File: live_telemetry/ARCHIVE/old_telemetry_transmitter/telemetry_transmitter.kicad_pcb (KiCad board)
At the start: 2 copper layers, 48.3 x 38.1 mm, 42 parts, among them J1 Programming Header, J2 BUS_CONN, J5 RFD900x, Q1 PJA3405, Q2 TSM2306CX, U1 PIC18F26K83, U2 MCP2562, U3 SPX3819M5-L-3-3/TR, U5 INA180, U6 AP1509-50SG-13, Y1 Crystal

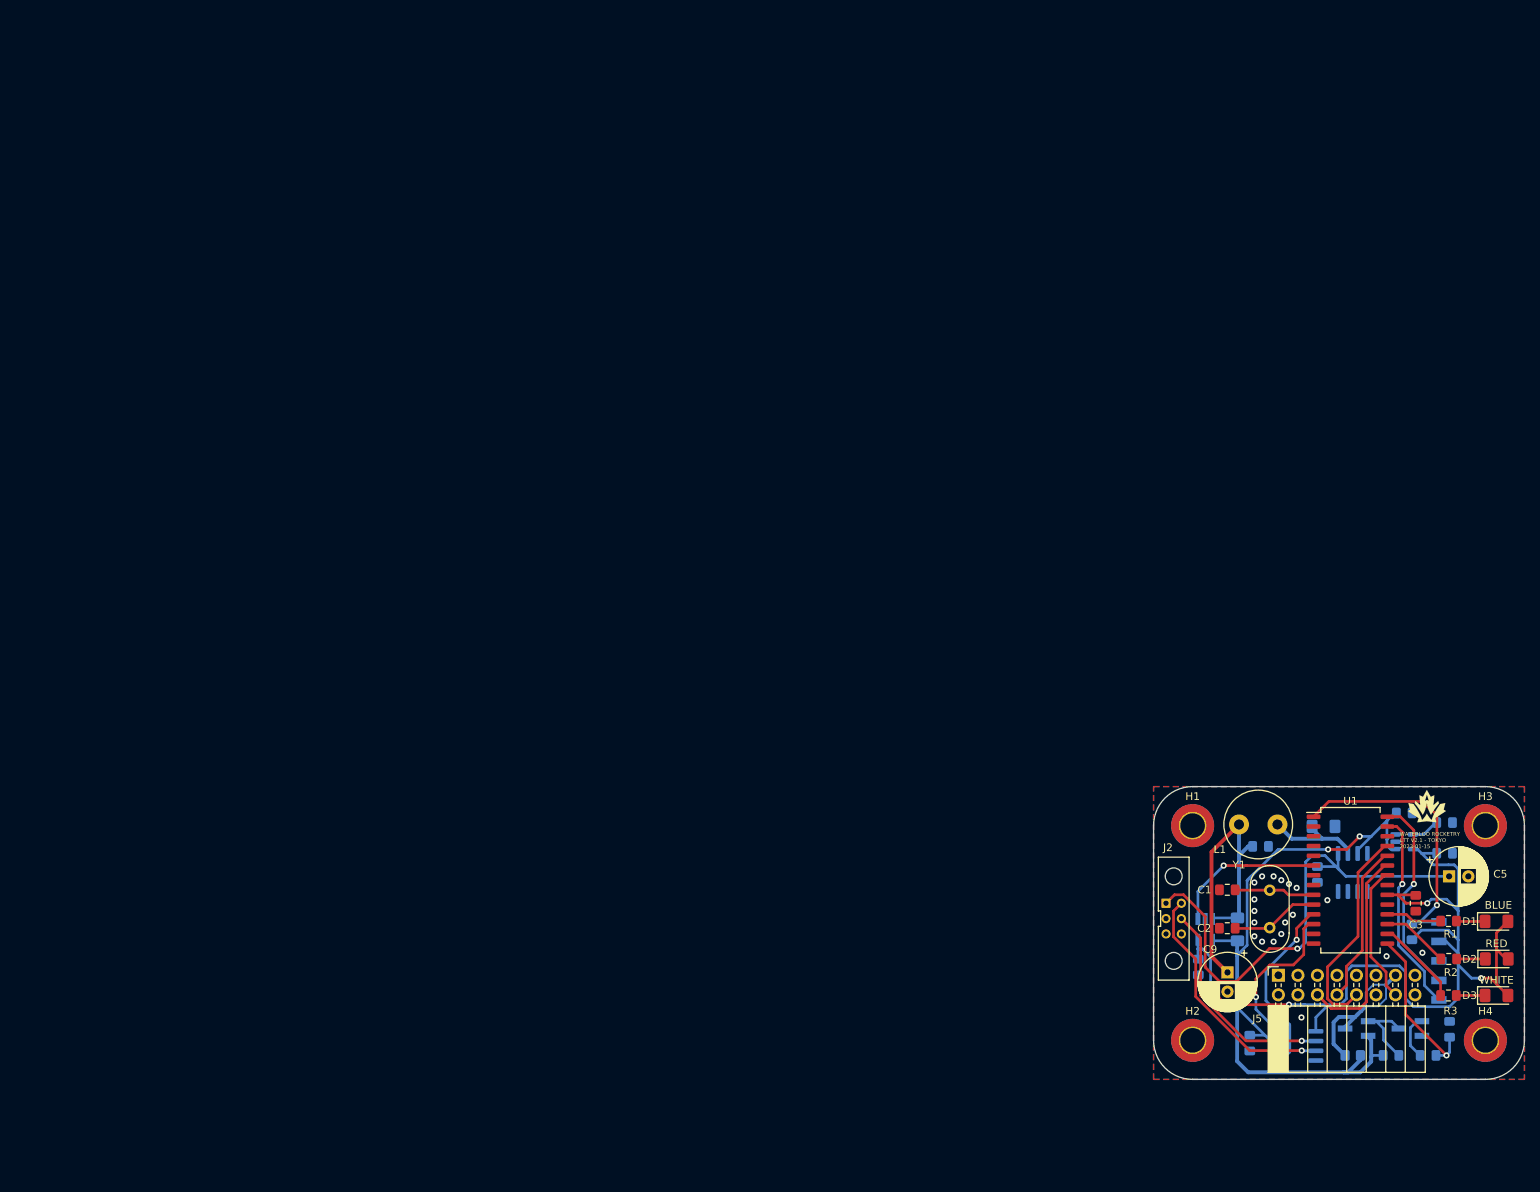
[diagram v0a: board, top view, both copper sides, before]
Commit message: add crystal and LDO datasheets, start layout
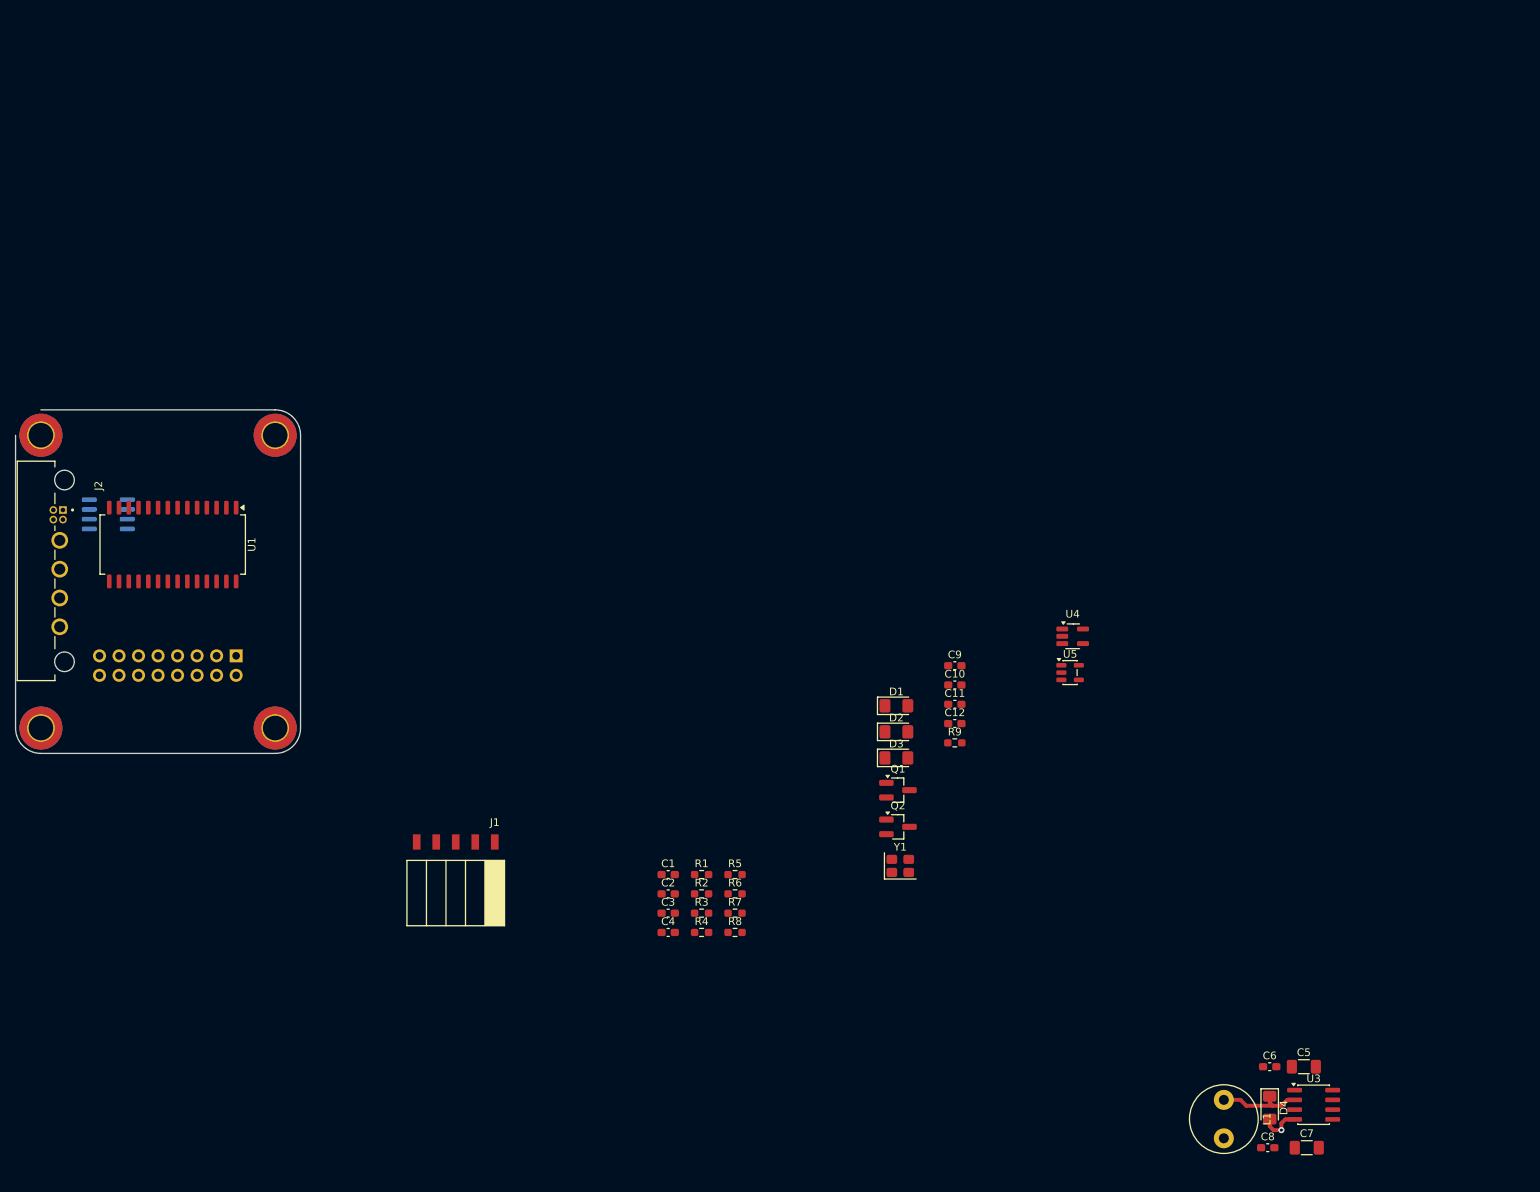
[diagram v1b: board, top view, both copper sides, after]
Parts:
- removed G***: LOGO, Team_Logo:Logo_SilkScreen_5mm
- removed J5: RFD900x, Connector_PinSocket_2.54mm:PinSocket_2x08_P2.54mm_Horizontal
- removed U6: AP1509-50SG-13, Package_SO:SOIC-8_3.9x4.9mm_P1.27mm
- added J3: RFD900x, Connector_PinSocket_2.54mm:PinSocket_2x08_P2.54mm_Horizontal, B.Cu at (63.5, 66.8)
- added U4: INA180, Package_TO_SOT_SMD:SOT-23-5_HandSoldering, F.Cu at (172.3, 64.3)
- C1, C2, C3: footprint Capacitor_SMD:C_0805_2012Metric_Pad1.15x1.40mm_HandSolder -> Capacitor_SMD:C_0603_1608Metric_Pad1.08x0.95mm_HandSolder
- C10: value 0.1u -> 10uF; footprint Capacitor_SMD:C_0805_2012Metric_Pad1.15x1.40mm_HandSolder -> Capacitor_SMD:C_0603_1608Metric_Pad1.08x0.95mm_HandSolder; moved to F.Cu
- C11: value 10uF -> 10nF; footprint Capacitor_SMD:C_0805_2012Metric_Pad1.15x1.40mm_HandSolder -> Capacitor_SMD:C_0603_1608Metric_Pad1.08x0.95mm_HandSolder; moved to F.Cu
- C12, C4, C6: footprint Capacitor_SMD:C_0805_2012Metric_Pad1.15x1.40mm_HandSolder -> Capacitor_SMD:C_0603_1608Metric_Pad1.08x0.95mm_HandSolder; moved to F.Cu
- C5: value 100u -> 22u; footprint Capacitor_THT:CP_Radial_D7.5mm_P2.50mm -> Capacitor_SMD:C_1206_3216Metric_Pad1.33x1.80mm_HandSolder
- C7: value 0.1u -> 22u; footprint Capacitor_SMD:C_0805_2012Metric_Pad1.15x1.40mm_HandSolder -> Capacitor_SMD:C_1206_3216Metric_Pad1.33x1.80mm_HandSolder; moved to F.Cu
- C8: value 10nF -> 0.1u; footprint Capacitor_SMD:C_0805_2012Metric_Pad1.15x1.40mm_HandSolder -> Capacitor_SMD:C_0603_1608Metric_Pad1.08x0.95mm_HandSolder; moved to F.Cu
- C9: value 100u -> 0.1u; footprint Capacitor_THT:CP_Radial_D7.5mm_P2.50mm -> Capacitor_SMD:C_0603_1608Metric_Pad1.08x0.95mm_HandSolder
- D4, Q1, Q2: moved to F.Cu
- J1: footprint canhw_footprints:PinHeader_5x2.54_SMD_90deg_952-3198-1-ND -> canhw_footprints:PinSocket_5x2.54_SMD_90deg_952-3198-1-ND; moved to F.Cu
- J2: value BUS_CONN -> G125-MH104M4-04AD000P; footprint canhw_footprints:connector_Harwin_M80-5000642 -> canhw_footprints:connector_Harwin_G125-MH104M4-04AD000P
- R1, R2, R3: footprint Resistor_SMD:R_0805_2012Metric_Pad1.15x1.40mm_HandSolder -> Resistor_SMD:R_0603_1608Metric_Pad0.98x0.95mm_HandSolder
- R4: footprint Resistor_SMD:R_0805_2012Metric_Pad1.15x1.40mm_HandSolder -> Resistor_SMD:R_0603_1608Metric_Pad0.98x0.95mm_HandSolder; moved to F.Cu
- R5: value 0.02R -> DNI; footprint Resistor_SMD:R_1206_3216Metric_Pad1.42x1.75mm_HandSolder -> Resistor_SMD:R_0603_1608Metric_Pad0.98x0.95mm_HandSolder; moved to F.Cu
- R6: value DNI -> 10K; footprint Resistor_SMD:R_0805_2012Metric_Pad1.20x1.40mm_HandSolder -> Resistor_SMD:R_0603_1608Metric_Pad0.98x0.95mm_HandSolder; moved to F.Cu
- R7: value 10K -> 130; footprint Resistor_SMD:R_0805_2012Metric_Pad1.15x1.40mm_HandSolder -> Resistor_SMD:R_0603_1608Metric_Pad0.98x0.95mm_HandSolder; moved to F.Cu
- R8: value 130 -> 10K; footprint Resistor_SMD:R_0805_2012Metric_Pad1.15x1.40mm_HandSolder -> Resistor_SMD:R_0603_1608Metric_Pad0.98x0.95mm_HandSolder; moved to F.Cu
- R9: value 10K -> 0.02R; footprint Resistor_SMD:R_0805_2012Metric_Pad1.15x1.40mm_HandSolder -> Resistor_SMD:R_0603_1608Metric_Pad0.98x0.95mm_HandSolder; moved to F.Cu
- U3: value SPX3819M5-L-3-3/TR -> AP1509-50SG-13; footprint Package_TO_SOT_SMD:SOT-23-5 -> Package_SO:SOIC-8_3.9x4.9mm_P1.27mm; moved to F.Cu
- U5: value INA180 -> SPX3819M5-L-3-3/TR; footprint Package_TO_SOT_SMD:SOT-23-5_HandSoldering -> Package_TO_SOT_SMD:SOT-23-5; moved to F.Cu
- Y1: value Crystal -> ABM8G-12.000MHZ-18-D2Y-T; footprint Crystal:Crystal_HC49-U_Vertical -> Crystal:Crystal_SMD_Abracon_ABM8G-4Pin_3.2x2.5mm
- moved H3 188.4 mm to (38.1, 76.2)
- moved U2 169.4 mm to (46.9, 48.4), turned to 180 degrees
- moved H4 162.6 mm to (68.6, 76.2)
- moved U1 159.4 mm to (55.2, 52.3), turned to -90 degrees
- moved H1 158.2 mm to (38.1, 38.1)
- moved J2 154.8 mm to (37.5, 55.8)
- moved H2 143.0 mm to (68.6, 38.1)
- moved J1 124.6 mm to (97.2, 91.0), turned to 180 degrees
- moved R3 97.8 mm to (124.1, 100.3), turned to 0 degrees
- moved R2 97.6 mm to (124.1, 97.8), turned to 0 degrees
- moved R1 97.4 mm to (124.1, 95.3), turned to 0 degrees
- moved C3 97.3 mm to (119.7, 100.3), turned to 0 degrees
- moved R4 92.4 mm to (124.1, 102.8), turned to 0 degrees
- moved R8 91.6 mm to (128.4, 102.8)
- moved R7 87.3 mm to (128.4, 100.3)
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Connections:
- C10 pad 2: Net-(C10-Pad2) -> +5V
- C11 pad 2: +5V -> Net-(U5-BP)
- C7 pad 1: GND -> /power/FB
- C7 pad 2: +3V3 -> GND
- C8 pad 2: Net-(C8-Pad2) -> /power/FB
- C9 pad 1: Net-(C10-Pad2) -> GND
- C9 pad 2: GND -> +3V3
- D4 pad 1: Net-(D4-Pad1) -> Net-(D4-K)
- J2 pad 1: +12V -> /CAN_H
- J2 pad 2: unconnected-(J2-Pad2) -> /CAN_L
- J2 pad 3: GND -> unconnected-(J2-NC-Pad3)
- J2 pad 4: /CAN_H -> unconnected-(J2-NC-Pad4)
- L1 pad 1: Net-(D4-Pad1) -> Net-(D4-K)
- L1 pad 2: Net-(C10-Pad2) -> /power/FB
- Q1 pad 1: Net-(Q1-Pad1) -> Net-(Q1-G)
- Q1 pad 3: Net-(J5-Pad13) -> Net-(J3-Pin_13)
- Q2 pad 1: Net-(Q2-Pad1) -> Net-(Q2-G)
- Q2 pad 3: Net-(Q1-Pad1) -> Net-(Q1-G)
- R5 pad 1: +5V -> Net-(J3-Pin_13)
- R5 pad 2: Net-(C10-Pad2) -> +5V
- R6 pad 1: Net-(J5-Pad13) -> +5V
- R6 pad 2: +5V -> Net-(Q1-G)
- R7 pad 1: +5V -> Net-(Q2-G)
- R7 pad 2: Net-(Q1-Pad1) -> /RADIO_OFF
- R8 pad 1: Net-(Q2-Pad1) -> /RADIO_OFF
- R8 pad 2: /RADIO_OFF -> GND
- R9 pad 1: /RADIO_OFF -> +5V
- R9 pad 2: GND -> /power/FB
- U3 pad 1: +5V -> +12V
- U3 pad 2: GND -> Net-(D4-K)
- U3 pad 3: +5V -> /power/FB
- U3 pad 4: Net-(C8-Pad2) -> GND
- U3 pad 5: +3V3 -> GND
- U5 pad 1: /power/CURR_LTT -> +5V
- U5 pad 3: Net-(C10-Pad2) -> +5V
- U5 pad 4: +5V -> Net-(U5-BP)
- Y1 pad 2: /OSC2 -> GND
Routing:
- net +3V3: track 122.7 -> 0.00 mm, vias 4 -> 0
- net +5V: track 100.1 -> 0.00 mm, vias 2 -> 0
- net +12V: track 64.4 -> 0.00 mm, vias 1 -> 0
- net Net-(C10-Pad2): track 39.4 -> 0.00 mm
- net /~{MCLR}: track 36.0 -> 0.00 mm, vias 1 -> 0
- net /CAN_H: track 32.3 -> 0.00 mm, vias 1 -> 0
- net /CAN_L: track 28.5 -> 0.00 mm, vias 1 -> 0
- net /RX: track 27.9 -> 0.00 mm
- net /RTS: track 26.5 -> 0.00 mm
- net /ICSPCLK: track 26.5 -> 0.00 mm, vias 1 -> 0
- net /ICSPDAT: track 26.2 -> 0.00 mm, vias 1 -> 0
- net /CAN_TX: track 24.0 -> 0.00 mm, vias 1 -> 0
- net Net-(J5-Pad13): track 23.5 -> 0.00 mm
- net /RADIO_OFF: track 21.7 -> 0.00 mm, vias 1 -> 0
- net /TX: track 21.1 -> 0.00 mm
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- removed copper zone on B.Cu, net GND
- removed copper zone on F.Cu, net GND
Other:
- board size 48.3 x 38.1 mm -> 37.1 x 44.7 mm
- board text removed: "BLUE"
- board text removed: "RED"
- board text removed: "WATERLOO ROCKETRY LTT V2.1 - TOKYO 2023-01-15"
- board text removed: "WHITE"
- board text removed: "~{MCLR}"

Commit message: finish layout and routing and add 3D models
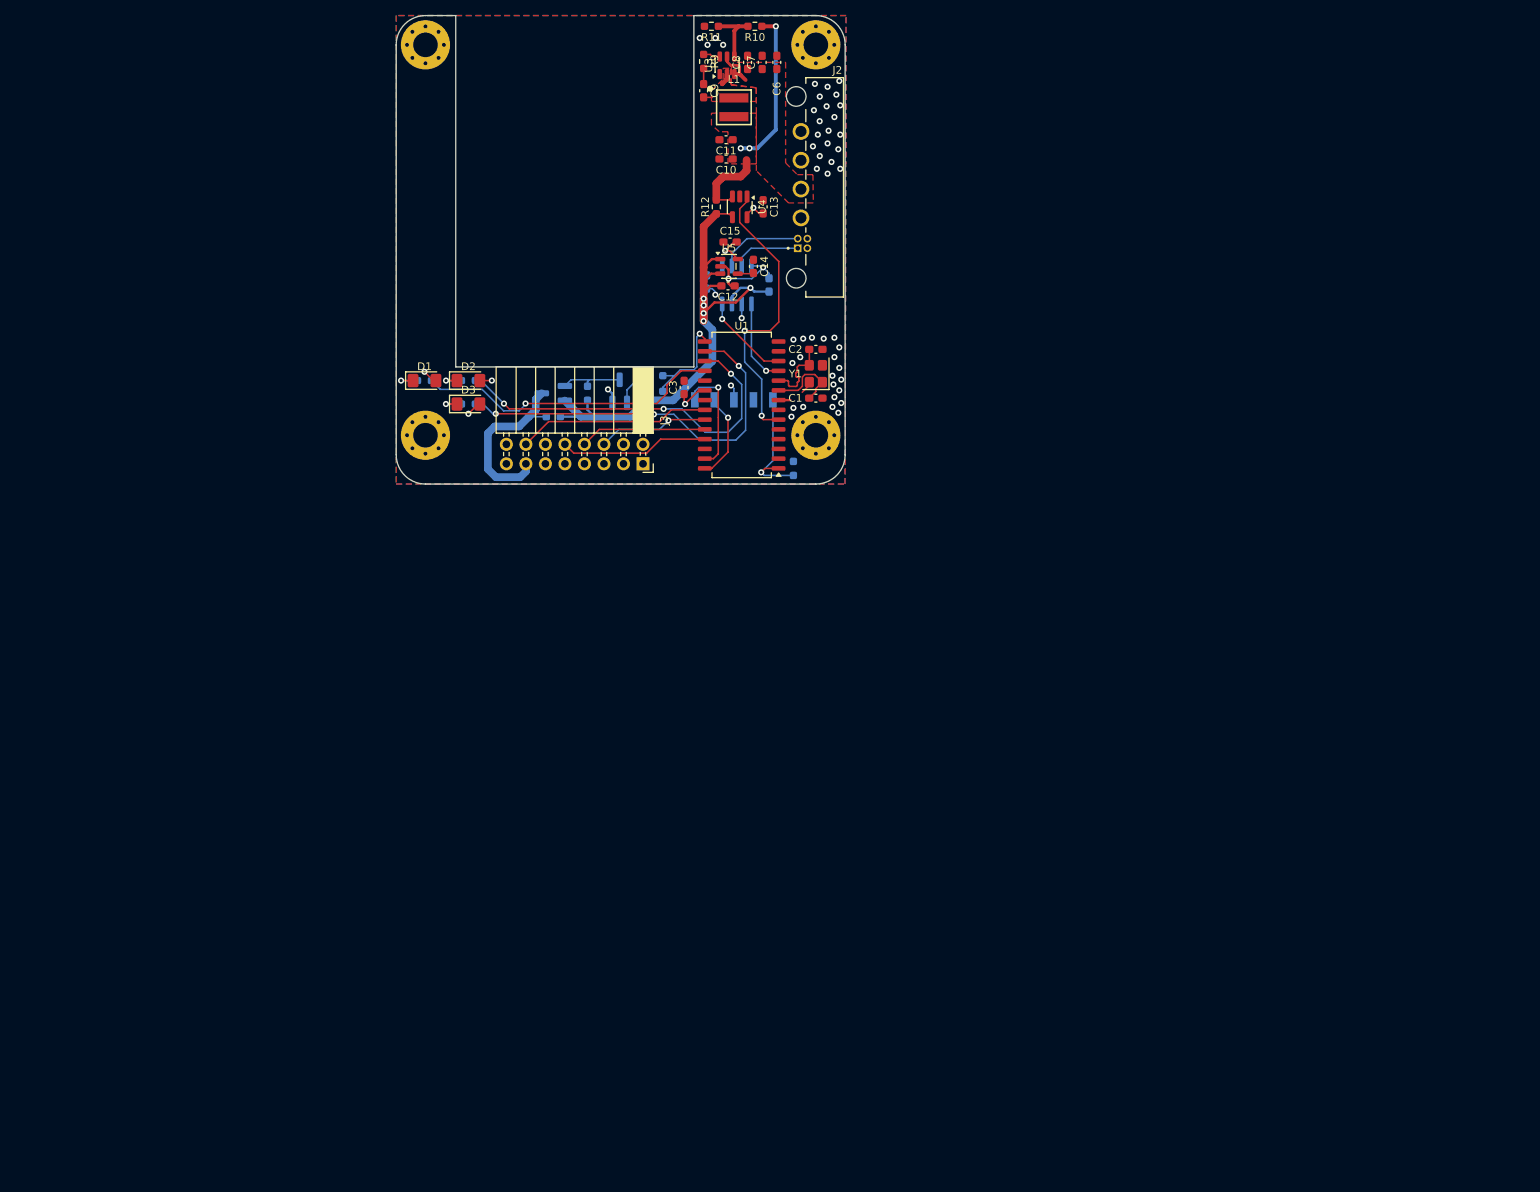
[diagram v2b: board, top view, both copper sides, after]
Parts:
- removed D4: SD1206S040S2R0, Diode_SMD:D_1206_3216Metric_Pad1.42x1.75mm_HandSolder
- added C13: 0.1u, Capacitor_SMD:C_0603_1608Metric_Pad1.08x0.95mm_HandSolder, F.Cu at (132.1, 8.38)
- added C14: 10nF, Capacitor_SMD:C_0603_1608Metric_Pad1.08x0.95mm_HandSolder, F.Cu at (130.8, 16.1)
- added C15: 2.2uF, Capacitor_SMD:C_0603_1608Metric_Pad1.08x0.95mm_HandSolder, F.Cu at (127.8, 13.0)
- added R10: 52.3k, Resistor_SMD:R_0603_1608Metric_Pad0.98x0.95mm_HandSolder, F.Cu at (131.0, -15.1)
- added R11: 10k, Resistor_SMD:R_0603_1608Metric_Pad0.98x0.95mm_HandSolder, F.Cu at (125.3, -15.1)
- added R12: 0.02R, Resistor_SMD:R_0603_1608Metric_Pad0.98x0.95mm_HandSolder, F.Cu at (126.0, 8.38)
- C10: value 10uF -> 22u
- C11: value 10nF -> 22u
- C12: value 2.2uF -> 10uF
- C4: value 10u -> 0.1u; moved to B.Cu
- C5: value 22u -> 0.1u; footprint Capacitor_SMD:C_1206_3216Metric_Pad1.33x1.80mm_HandSolder -> Capacitor_SMD:C_0603_1608Metric_Pad1.08x0.95mm_HandSolder; moved to B.Cu
- C6: value 0.1u -> 10u
- C7: value 22u -> 10u; footprint Capacitor_SMD:C_1206_3216Metric_Pad1.33x1.80mm_HandSolder -> Capacitor_SMD:C_0603_1608Metric_Pad1.08x0.95mm_HandSolder
- C8, C9: value 0.1u -> 100n
- H1, H2, H3, H4: footprint MountingHole:MountingHole_3.2mm_M3_DIN965_Pad_TopBottom -> MountingHole:MountingHole_3.2mm_M3_Pad_Via; moved to B.Cu
- J1, Q1, Q2, R1, R2, R3, R4, R5, R6, R7, R8: moved to B.Cu
- J3: moved to F.Cu
- L1: value 47u -> 74439325056; footprint Inductor_THT:L_Radial_D8.7mm_P5.00mm_Fastron_07HCP -> telemetry_transmitter:WE-XHMI_4040
- R9: value 0.02R -> 30R
- U3: value AP1509-50SG-13 -> TPS56339DDC; footprint Package_SO:SOIC-8_3.9x4.9mm_P1.27mm -> Package_TO_SOT_SMD:SOT-23-6
- moved C7 158.0 mm to (132.0, -10.4), turned to 90 degrees
- moved C8 156.6 mm to (130.0, -10.4), turned to 90 degrees
- moved U3 155.3 mm to (127.4, -10.0), turned to 90 degrees
- moved C6 145.6 mm to (133.9, -10.4), turned to 90 degrees
- moved L1 144.0 mm to (128.3, -4.57), turned to 0 degrees
- moved C5 123.3 mm to (132.8, 18.5), turned to 90 degrees
- moved J2 114.1 mm to (140.1, 5.84), turned to 90 degrees
- moved H4 113.4 mm to (138.9, -12.7), turned to 180 degrees
- moved H3 102.0 mm to (88.1, -12.7), turned to 180 degrees
- moved R9 94.5 mm to (124.3, -10.5), turned to -90 degrees
- moved U2 87.1 mm to (128.7, 18.5), turned to 90 degrees
- moved C4 84.8 mm to (124.7, 18.2), turned to -90 degrees
- moved C9 81.6 mm to (124.3, -6.73), turned to -90 degrees
- moved C11 79.3 mm to (127.3, -0.35), turned to 180 degrees
- moved U1 76.2 mm to (129.3, 34.2), turned to 180 degrees
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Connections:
- C10 pad 1: GND -> Net-(U4-IN+)
- C10 pad 2: +5V -> GND
- C11 pad 1: GND -> Net-(U4-IN+)
- C11 pad 2: Net-(U5-BP) -> GND
- C12 pad 2: +3V3 -> +5V
- C4 pad 1: +5V -> +3V3
- C5 pad 1: +12V -> +5V
- C6 pad 1: GND -> +12V
- C6 pad 2: +12V -> GND
- C7 pad 1: /power/FB -> +12V
- C8 pad 1: GND -> +12V
- C8 pad 2: /power/FB -> GND
- C9 pad 1: GND -> Net-(C9-Pad1)
- C9 pad 2: +3V3 -> Net-(U3-SW)
- H1 pad 1: unconnected-(H1-Pad1)_2 -> GND
- H2 pad 1: unconnected-(H2-Pad1)_1 -> GND
- H3 pad 1: unconnected-(H3-Pad1)_1 -> GND
- H4 pad 1: unconnected-(H4-Pad1)_2 -> GND
- L1 pad 1: Net-(D4-K) -> Net-(U3-SW)
- L1 pad 2: /power/FB -> Net-(U4-IN+)
- R9 pad 1: +5V -> /power/BOOT
- R9 pad 2: /power/FB -> Net-(C9-Pad1)
- U3 pad 1: +12V -> GND
- U3 pad 2: Net-(D4-K) -> Net-(U3-SW)
- U3 pad 3: /power/FB -> +12V
- U3 pad 4: GND -> Net-(U3-FB)
- U3 pad 5: GND -> +12V
- U3 pad 6: GND -> /power/BOOT
- U4 pad 3: /power/FB -> Net-(U4-IN+)
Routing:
- net +5V: track 0.00 -> 75.5 mm, vias 0 -> 5
- net /LED3: track 0.00 -> 51.6 mm, vias 0 -> 3
- net /LED2: track 0.00 -> 48.7 mm, vias 0 -> 3
- net /LED1: track 0.00 -> 40.1 mm, vias 0 -> 1
- net /power/CURR_LTT: track 0.00 -> 38.3 mm, vias 0 -> 2
- net Net-(U4-IN+): track 0.00 -> 31.3 mm, vias 0 -> 3
- net /CTS: track 0.00 -> 25.1 mm
- net Net-(J3-Pin_13): track 0.00 -> 23.6 mm
- net /RX: track 0.00 -> 19.4 mm
- net GND: track 5.48 -> 24.9 mm, vias 1 -> 53
- net +3V3: track 0.00 -> 17.4 mm, vias 0 -> 6
- net /~{MCLR}: track 0.00 -> 16.9 mm, vias 0 -> 1
- net /TX: track 0.00 -> 16.5 mm
- net /ICSPCLK: track 0.00 -> 15.0 mm, vias 0 -> 1
- net /RTS: track 0.00 -> 14.5 mm, vias 0 -> 1
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- added copper zone on F.Cu, net +12V
- added copper zone on B.Cu, net +3V3
- added copper zone on F.Cu, net GND
- added copper zone on F.Cu, net Net-(U3-SW)
- added copper zone on F.Cu, net Net-(U4-IN+)
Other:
- board size 37.1 x 44.7 mm -> 58.4 x 61 mm
